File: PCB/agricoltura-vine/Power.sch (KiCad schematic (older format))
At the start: 17 parts, among them T16 1755736, U4 AP63203WU-7, U5 AP63205WU-7

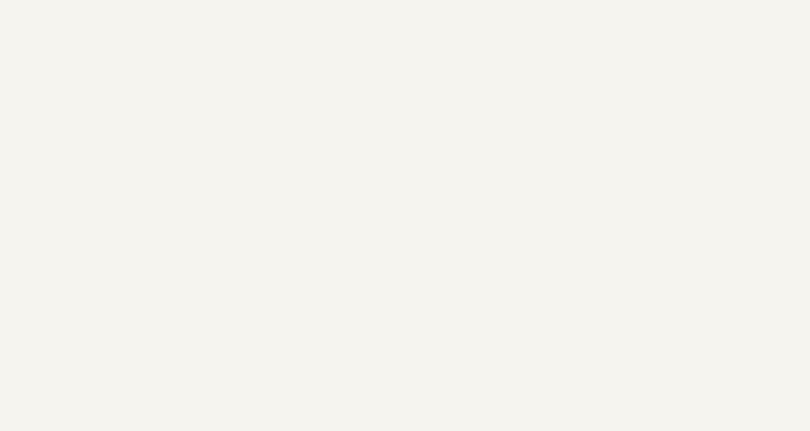
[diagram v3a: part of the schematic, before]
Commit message: Board Size , Connectors and Layout
Changed board size and shape, started layout, swapped connectors over.
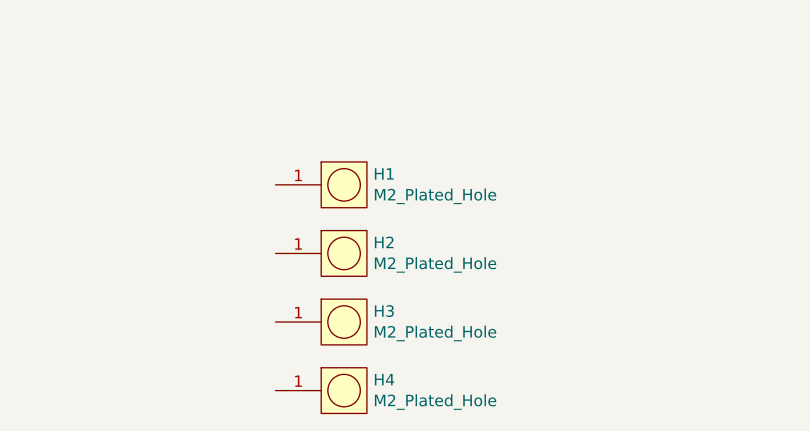
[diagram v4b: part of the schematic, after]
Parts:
- added H1, H2, H3, H4: M2_Plated_Hole, AVR-KiCAD-Lib-Holes_Fasteners:M2_HOLE, symbol AVR-KiCAD-Lib-Holes_Fasteners:M2_Plated_Hole
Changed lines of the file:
@@
 Wire Wire Line
 	4600 3500 4800 3500
+$Comp
+L AVR-KiCAD-Lib-Holes_Fasteners:M2_Plated_Hole H1
+U 1 1 5F227FD5
+P 2750 5600
+F 0 "H1" H 2978 5646 50  0000 L CNN
+F 1 "M2_Plated_Hole" H 2978 5555 50  0000 L CNN
+F 2 "AVR-KiCAD-Lib-Holes_Fasteners:M2_HOLE" H 2750 5600 50  0001 C CNN
+F 3 "" H 2750 5600 50  0001 C CNN
+F 4 "*" H 2850 5850 50  0001 C CNN "Cost QTY: 1"
+F 5 "*" H 2950 5950 50  0001 C CNN "Cost QTY: 1000"
+F 6 "*" H 3050 6050 50  0001 C CNN "Cost QTY: 2500"
+F 7 "*" H 3150 6150 50  0001 C CNN "Cost QTY: 5000"
+F 8 "*" H 3250 6250 50  0001 C CNN "Cost QTY: 10000"
+F 9 "*" H 3350 6350 50  0001 C CNN "MFR"
+F 10 "*" H 3450 6450 50  0001 C CNN "MFR#"
+F 11 "*" H 3550 6550 50  0001 C CNN "Vendor"
+F 12 "*" H 3650 6650 50  0001 C CNN "Vendor #"
+F 13 "*" H 3750 6750 50  0001 C CNN "Designer"
+F 14 "*" H 3850 6850 50  0001 C CNN "Height"
+F 15 "*" H 4950 7950 50  0001 C CNN "Date Created"
+F 16 "*" H 3950 6950 50  0001 C CNN "Date Modified"
+F 17 "*" H 4050 7050 50  0001 C CNN "Lead-Free ?"
+F 18 "*" H 4150 7150 50  0001 C CNN "RoHS Levels"
+F 19 "*" H 4250 7250 50  0001 C CNN "Mounting"
+F 20 "*" H 4350 7350 50  0001 C CNN "Pin Count #"
+F 21 "*" H 4450 7450 50  0001 C CNN "Status"
+F 22 "*" H 4550 7550 50  0001 C CNN "Tolerance"
+F 23 "*" H 4650 7650 50  0001 C CNN "Type"
+F 24 "*" H 4750 7750 50  0001 C CNN "Voltage"
+F 25 "*" H 4850 7900 50  0001 C CNN "Package"
+F 26 "M2 Hole" H 5050 8100 50  0001 C CNN "_Value_"
+F 27 "*" H 5150 8200 50  0001 C CNN "Management_ID"
+F 28 "Plated M2 Screw Hole" H 5150 8200 50  0001 C CNN "Description"
+	1    2750 5600
+	1    0    0    -1
+$EndComp
+$Comp
+L AVR-KiCAD-Lib-Holes_Fasteners:M2_Plated_Hole H2
+U 1 1 5F22DFB9
+P 2750 5900
+F 0 "H2" H 2978 5946 50  0000 L CNN
+F 1 "M2_Plated_Hole" H 2978 5855 50  0000 L CNN
+F 2 "AVR-KiCAD-Lib-Holes_Fasteners:M2_HOLE" H 2750 5900 50  0001 C CNN
+F 3 "" H 2750 5900 50  0001 C CNN
+F 4 "*" H 2850 6150 50  0001 C CNN "Cost QTY: 1"
+F 5 "*" H 2950 6250 50  0001 C CNN "Cost QTY: 1000"
+F 6 "*" H 3050 6350 50  0001 C CNN "Cost QTY: 2500"
+F 7 "*" H 3150 6450 50  0001 C CNN "Cost QTY: 5000"
+F 8 "*" H 3250 6550 50  0001 C CNN "Cost QTY: 10000"
+F 9 "*" H 3350 6650 50  0001 C CNN "MFR"
+F 10 "*" H 3450 6750 50  0001 C CNN "MFR#"
+F 11 "*" H 3550 6850 50  0001 C CNN "Vendor"
+F 12 "*" H 3650 6950 50  0001 C CNN "Vendor #"
+F 13 "*" H 3750 7050 50  0001 C CNN "Designer"
+F 14 "*" H 3850 7150 50  0001 C CNN "Height"
+F 15 "*" H 4950 8250 50  0001 C CNN "Date Created"
+F 16 "*" H 3950 7250 50  0001 C CNN "Date Modified"
+F 17 "*" H 4050 7350 50  0001 C CNN "Lead-Free ?"
+F 18 "*" H 4150 7450 50  0001 C CNN "RoHS Levels"
+F 19 "*" H 4250 7550 50  0001 C CNN "Mounting"
+F 20 "*" H 4350 7650 50  0001 C CNN "Pin Count #"
+F 21 "*" H 4450 7750 50  0001 C CNN "Status"
+F 22 "*" H 4550 7850 50  0001 C CNN "Tolerance"
+F 23 "*" H 4650 7950 50  0001 C CNN "Type"
+F 24 "*" H 4750 8050 50  0001 C CNN "Voltage"
+F 25 "*" H 4850 8200 50  0001 C CNN "Package"
+F 26 "M2 Hole" H 5050 8400 50  0001 C CNN "_Value_"
+F 27 "*" H 5150 8500 50  0001 C CNN "Management_ID"
+F 28 "Plated M2 Screw Hole" H 5150 8500 50  0001 C CNN "Description"
+	1    2750 5900
+	1    0    0    -1
+$EndComp
+$Comp
+L AVR-KiCAD-Lib-Holes_Fasteners:M2_Plated_Hole H3
+U 1 1 5F22E952
+P 2750 6200
+F 0 "H3" H 2978 6246 50  0000 L CNN
+F 1 "M2_Plated_Hole" H 2978 6155 50  0000 L CNN
+F 2 "AVR-KiCAD-Lib-Holes_Fasteners:M2_HOLE" H 2750 6200 50  0001 C CNN
+F 3 "" H 2750 6200 50  0001 C CNN
+F 4 "*" H 2850 6450 50  0001 C CNN "Cost QTY: 1"
+F 5 "*" H 2950 6550 50  0001 C CNN "Cost QTY: 1000"
+F 6 "*" H 3050 6650 50  0001 C CNN "Cost QTY: 2500"
+F 7 "*" H 3150 6750 50  0001 C CNN "Cost QTY: 5000"
+F 8 "*" H 3250 6850 50  0001 C CNN "Cost QTY: 10000"
+F 9 "*" H 3350 6950 50  0001 C CNN "MFR"
+F 10 "*" H 3450 7050 50  0001 C CNN "MFR#"
+F 11 "*" H 3550 7150 50  0001 C CNN "Vendor"
+F 12 "*" H 3650 7250 50  0001 C CNN "Vendor #"
+F 13 "*" H 3750 7350 50  0001 C CNN "Designer"
+F 14 "*" H 3850 7450 50  0001 C CNN "Height"
+F 15 "*" H 4950 8550 50  0001 C CNN "Date Created"
+F 16 "*" H 3950 7550 50  0001 C CNN "Date Modified"
+F 17 "*" H 4050 7650 50  0001 C CNN "Lead-Free ?"
+F 18 "*" H 4150 7750 50  0001 C CNN "RoHS Levels"
+F 19 "*" H 4250 7850 50  0001 C CNN "Mounting"
+F 20 "*" H 4350 7950 50  0001 C CNN "Pin Count #"
+F 21 "*" H 4450 8050 50  0001 C CNN "Status"
+F 22 "*" H 4550 8150 50  0001 C CNN "Tolerance"
+F 23 "*" H 4650 8250 50  0001 C CNN "Type"
+F 24 "*" H 4750 8350 50  0001 C CNN "Voltage"
+F 25 "*" H 4850 8500 50  0001 C CNN "Package"
+F 26 "M2 Hole" H 5050 8700 50  0001 C CNN "_Value_"
+F 27 "*" H 5150 8800 50  0001 C CNN "Management_ID"
+F 28 "Plated M2 Screw Hole" H 5150 8800 50  0001 C CNN "Description"
+	1    2750 6200
+	1    0    0    -1
+$EndComp
+$Comp
+L AVR-KiCAD-Lib-Holes_Fasteners:M2_Plated_Hole H4
+U 1 1 5F22F019
+P 2750 6500
+F 0 "H4" H 2978 6546 50  0000 L CNN
+F 1 "M2_Plated_Hole" H 2978 6455 50  0000 L CNN
+F 2 "AVR-KiCAD-Lib-Holes_Fasteners:M2_HOLE" H 2750 6500 50  0001 C CNN
+F 3 "" H 2750 6500 50  0001 C CNN
+F 4 "*" H 2850 6750 50  0001 C CNN "Cost QTY: 1"
+F 5 "*" H 2950 6850 50  0001 C CNN "Cost QTY: 1000"
+F 6 "*" H 3050 6950 50  0001 C CNN "Cost QTY: 2500"
+F 7 "*" H 3150 7050 50  0001 C CNN "Cost QTY: 5000"
+F 8 "*" H 3250 7150 50  0001 C CNN "Cost QTY: 10000"
+F 9 "*" H 3350 7250 50  0001 C CNN "MFR"
+F 10 "*" H 3450 7350 50  0001 C CNN "MFR#"
+F 11 "*" H 3550 7450 50  0001 C CNN "Vendor"
+F 12 "*" H 3650 7550 50  0001 C CNN "Vendor #"
+F 13 "*" H 3750 7650 50  0001 C CNN "Designer"
+F 14 "*" H 3850 7750 50  0001 C CNN "Height"
+F 15 "*" H 4950 8850 50  0001 C CNN "Date Created"
+F 16 "*" H 3950 7850 50  0001 C CNN "Date Modified"
+F 17 "*" H 4050 7950 50  0001 C CNN "Lead-Free ?"
+F 18 "*" H 4150 8050 50  0001 C CNN "RoHS Levels"
+F 19 "*" H 4250 8150 50  0001 C CNN "Mounting"
+F 20 "*" H 4350 8250 50  0001 C CNN "Pin Count #"
+F 21 "*" H 4450 8350 50  0001 C CNN "Status"
+F 22 "*" H 4550 8450 50  0001 C CNN "Tolerance"
+F 23 "*" H 4650 8550 50  0001 C CNN "Type"
+F 24 "*" H 4750 8650 50  0001 C CNN "Voltage"
+F 25 "*" H 4850 8800 50  0001 C CNN "Package"
+F 26 "M2 Hole" H 5050 9000 50  0001 C CNN "_Value_"
+F 27 "*" H 5150 9100 50  0001 C CNN "Management_ID"
+F 28 "Plated M2 Screw Hole" H 5150 9100 50  0001 C CNN "Description"
+	1    2750 6500
+	1    0    0    -1
+$EndComp
 $EndSCHEMATC

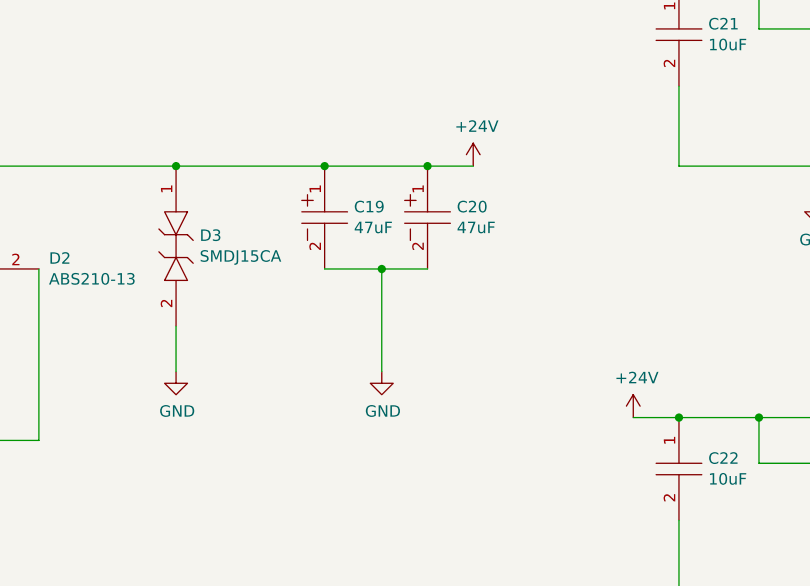
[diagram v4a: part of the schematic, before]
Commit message: Board shape and Rough PLacement
Board shape adjusted to have smaller rounded corners increasing usable space of board shape. Finished rough placement of all the components, no routing yet. Debating connector style and form factor. Right now supports Seeedstudio grove connectors, contemplating Sparkfun Qwiic  and Adafruit Stemma connectors as alternatives or including a variety of all 3.
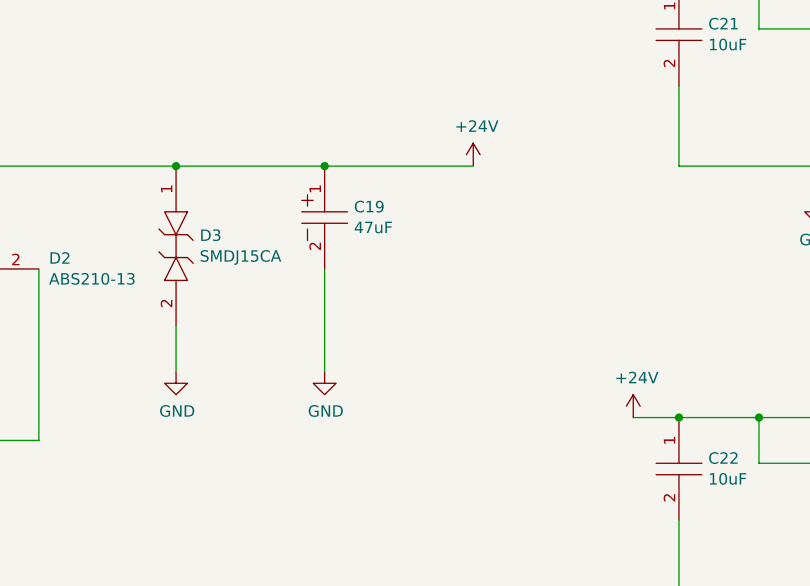
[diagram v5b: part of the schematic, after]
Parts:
- removed C20: UUQ1H470MCL1GS, AVR-KiCAD-Lib-Capacitors:CP_Elec_8x10, symbol AVR-KiCAD-Lib-Capacitors:UUQ1H470MCL1GS
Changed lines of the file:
@@
 $EndComp
 Connection ~ 4350 3050
-Wire Wire Line
-	4350 3050 4800 3050
-$Comp
-L AVR-KiCAD-Lib-Capacitors:UUQ1H470MCL1GS C20
-U 1 1 5EF7802F
-P 4800 3250
-F 0 "C20" V 4779 3378 50  0000 L CNN
-F 1 "UUQ1H470MCL1GS" H 4850 3450 50  0001 C CNN
-F 2 "AVR-KiCAD-Lib-Capacitors:CP_Elec_8x10" H 4600 3250 50  0001 C CNN
-F 3 "https://www.nichicon.co.jp/english/products/pdfs/e-uuq.pdf" H 4700 3350 50  0001 C CNN
-F 4 "1.06000" H 4900 3500 50  0001 C CNN "Cost QTY: 1"
-F 5 "*" H 5000 3600 50  0001 C CNN "Cost QTY: 1000"
-F 6 "*" H 5100 3700 50  0001 C CNN "Cost QTY: 2500"
-F 7 "*" H 5200 3800 50  0001 C CNN "Cost QTY: 5000"
-F 8 "*" H 5300 3900 50  0001 C CNN "Cost QTY: 10000"
-F 9 "Nichicon" H 5400 4000 50  0001 C CNN "MFR"
-F 10 "UUQ1H470MCL1GS" H 5500 4100 50  0001 C CNN "MFR#"
-F 11 "Digikey" H 5600 4200 50  0001 C CNN "Vendor"
-F 12 "493-3212-1-ND" H 5700 4300 50  0001 C CNN "Vendor #"
-F 13 "AVR" H 5800 4400 50  0001 C CNN "Designer"
-F 14 "6.2mm" H 5900 4500 50  0001 C CNN "Height"
-F 15 "12/16/2019" H 7000 5600 50  0001 C CNN "Date Created"
-F 16 "12/16/2019" H 6000 4600 50  0001 C CNN "Date Modified"
-F 17 "Yes" H 6100 4700 50  0001 C CNN "Lead-Free ?"
-F 18 "1" H 6200 4800 50  0001 C CNN "RoHS Levels"
-F 19 "SMT" H 6300 4900 50  0001 C CNN "Mounting"
-F 20 "2" H 6400 5000 50  0001 C CNN "Pin Count #"
-F 21 "Active" H 6500 5100 50  0001 C CNN "Status"
-F 22 "20%" H 6600 5200 50  0001 C CNN "Tolerance"
-F 23 "Alu  Cap Audio" H 6700 5300 50  0001 C CNN "Type"
-F 24 "50V" H 6800 5400 50  0001 C CNN "Voltage"
-F 25 "Radial SMD" H 6900 5550 50  0001 C CNN "Package"
-F 26 "47µF 50V Aluminum Electrolytic Capacitors Radial, Can - SMD 1000 Hrs @ 105°C" H 7300 5950 50  0001 C CNN "Description"
-F 27 "47uF" V 4870 3378 50  0000 L CNN "_Value_"
-F 28 "*" H 7200 5850 50  0001 C CNN "Management_ID"
-	1    4800 3250
-	0    1    1    0
-$EndComp
-Connection ~ 4800 3050
-Wire Wire Line
-	4800 3050 5000 3050
 $Comp
 L power:GND #PWR030
 U 1 1 5EF78FAF
-P 4600 3950
-F 0 "#PWR030" H 4600 3700 50  0001 C CNN
-F 1 "GND" H 4605 3777 50  0000 C CNN
-F 2 "" H 4600 3950 50  0001 C CNN
-F 3 "" H 4600 3950 50  0001 C CNN
-	1    4600 3950
+P 4350 3950
+F 0 "#PWR030" H 4350 3700 50  0001 C CNN
+F 1 "GND" H 4355 3777 50  0000 C CNN
+F 2 "" H 4350 3950 50  0001 C CNN
+F 3 "" H 4350 3950 50  0001 C CNN
+	1    4350 3950
 	1    0    0    -1
 $EndComp
 Wire Wire Line
-	4350 3500 4600 3500
-Wire Wire Line
-	4600 3950 4600 3500
-Connection ~ 4600 3500
-Wire Wire Line
-	4600 3500 4800 3500
+	4350 3950 4350 3500
 $Comp
 L AVR-KiCAD-Lib-Holes_Fasteners:M2_Plated_Hole H1
@@
 	1    0    0    -1
 $EndComp
+Wire Wire Line
+	4350 3050 5000 3050
 $EndSCHEMATC

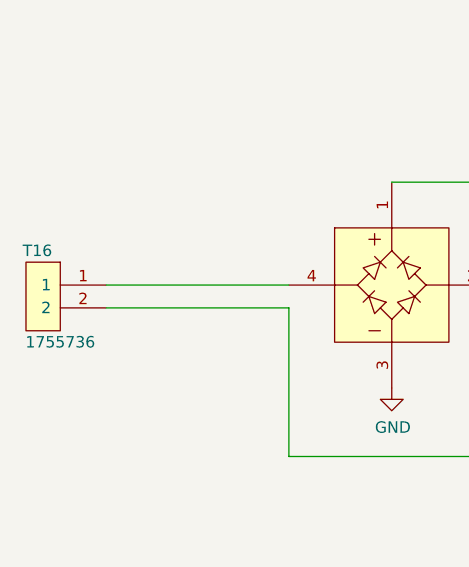
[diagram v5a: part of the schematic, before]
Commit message: Route Started Connectors Changed
Changed to QWIIC style connectors and adjusted pinning of RJ45s, but switching to screw terminal header in next commit. THis is a backup
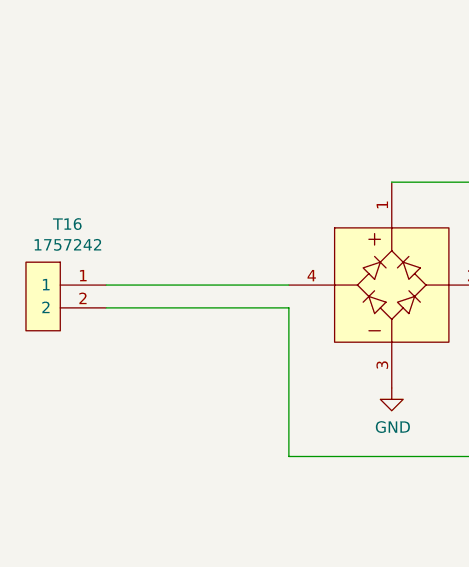
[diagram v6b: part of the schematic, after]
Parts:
- removed T16: 1755736, growbox-KiCAD-Connectors:PhoenixContact_MSTBVA-G_02x5.08mm_Vertical, symbol AVR-KiCAD-Lib-Connectors:1755736
- added T16: 1757242, AVR-KiCAD-Lib-Connectors:PhoenixContact_MSTBA-G_02x5.08mm_Angled, symbol AVR-KiCAD-Lib-Connectors:1757242
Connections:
- net at D2.4: now also T16.1
- net at D2.2: now also T16.2
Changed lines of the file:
@@
 $EndDescr
-$Comp
-L AVR-KiCAD-Lib-Connectors:1755736 T16
-U 1 1 5EEBB45B
-P 1200 3300
-F 0 "T16" H 1300 3250 50  0000 C CNN
-F 1 "1755736" H 1200 2850 50  0000 C CNN
-F 2 "growbox-KiCAD-Connectors:PhoenixContact_MSTBVA-G_02x5.08mm_Vertical" H 1000 3300 50  0001 C CNN
-F 3 "https://media.digikey.com/pdf/Data%20Sheets/Phoenix%20Contact%20PDFs/1755794.pdf" H 1100 3400 50  0001 C CNN
-F 4 "0.64000" H 1300 3550 50  0001 C CNN "Cost QTY: 1"
-F 5 "0.45518" H 1400 3650 50  0001 C CNN "Cost QTY: 1000"
-F 6 "0.43375" H 1500 3750 50  0001 C CNN "Cost QTY: 2500"
-F 7 "0.40698" H 1600 3850 50  0001 C CNN "Cost QTY: 5000"
-F 8 "*" H 1700 3950 50  0001 C CNN "Cost QTY: 10000"
-F 9 "Phoenix Contact" H 1800 4050 50  0001 C CNN "MFR"
-F 10 "1755736" H 1900 4150 50  0001 C CNN "MFR#"
-F 11 "Digikey" H 2000 4250 50  0001 C CNN "Vendor"
-F 12 "277-1150-ND" H 2100 4350 50  0001 C CNN "Vendor #"
-F 13 "AVR" H 2200 4450 50  0001 C CNN "Designer"
-F 14 "12mm" H 2300 4550 50  0001 C CNN "Height"
-F 15 "3/11/2020" H 3400 5650 50  0001 C CNN "Date Created"
-F 16 "3/11/2020" H 2400 4650 50  0001 C CNN "Date Modified"
-F 17 "Yes" H 2500 4750 50  0001 C CNN "Lead-Free ?"
-F 18 "1" H 2600 4850 50  0001 C CNN "RoHS Levels"
-F 19 "ThroughHole" H 2700 4950 50  0001 C CNN "Mounting"
-F 20 "2" H 2800 5050 50  0001 C CNN "Pin Count #"
-F 21 "Active" H 2900 5150 50  0001 C CNN "Status"
-F 22 "*" H 3000 5250 50  0001 C CNN "Tolerance"
-F 23 "Connector, Terminal Block " H 3100 5350 50  0001 C CNN "Type"
-F 24 "300V" H 3200 5450 50  0001 C CNN "Voltage"
-F 25 "*" H 3300 5600 50  0001 C CNN "Package"
-F 26 "2 Position Terminal Block Header, Male Pins, Shrouded (4 Side) 0.200\" (5.08mm) Vertical  Through Hole" H 3700 6000 50  0001 C CNN "Description"
-F 27 "1755736" H 3500 5800 50  0001 C CNN "_Value_"
-F 28 "*" H 3600 5900 50  0001 C CNN "Management_ID"
-	1    1200 3300
-	-1   0    0    -1
-$EndComp
 $Comp
 L AVR-KiCAD-Lib-Diodes:ABS210-13 D2
@@
 Wire Wire Line
 	4350 3050 5000 3050
+$Comp
+L AVR-KiCAD-Lib-Connectors:1757242 T16
+U 1 1 5EF359F8
+P 1200 3300
+F 0 "T16" H 1167 3365 50  0000 C CNN
+F 1 "1757242" H 1167 3274 50  0000 C CNN
+F 2 "AVR-KiCAD-Lib-Connectors:PhoenixContact_MSTBA-G_02x5.08mm_Angled" H 1000 3300 50  0001 C CNN
+F 3 "https://media.digikey.com/pdf/Data%20Sheets/Phoenix%20Contact%20PDFs/1757242.pdf" H 1100 3400 50  0001 C CNN
+F 4 "0.64000" H 1300 3550 50  0001 C CNN "Cost QTY: 1"
+F 5 "0.45518" H 1400 3650 50  0001 C CNN "Cost QTY: 1000"
+F 6 "0.43375" H 1500 3750 50  0001 C CNN "Cost QTY: 2500"
+F 7 "0.40698" H 1600 3850 50  0001 C CNN "Cost QTY: 5000"
+F 8 "*" H 1700 3950 50  0001 C CNN "Cost QTY: 10000"
+F 9 "Phoenix Contact" H 1800 4050 50  0001 C CNN "MFR"
+F 10 "1757242" H 1900 4150 50  0001 C CNN "MFR#"
+F 11 "Digikey" H 2000 4250 50  0001 C CNN "Vendor"
+F 12 "277-1106-ND" H 2100 4350 50  0001 C CNN "Vendor #"
+F 13 "AVR" H 2200 4450 50  0001 C CNN "Designer"
+F 14 "12mm" H 2300 4550 50  0001 C CNN "Height"
+F 15 "6/20/2020" H 3400 5650 50  0001 C CNN "Date Created"
+F 16 "6/20/2020" H 2400 4650 50  0001 C CNN "Date Modified"
+F 17 "Yes" H 2500 4750 50  0001 C CNN "Lead-Free ?"
+F 18 "1" H 2600 4850 50  0001 C CNN "RoHS Levels"
+F 19 "ThroughHole" H 2700 4950 50  0001 C CNN "Mounting"
+F 20 "2" H 2800 5050 50  0001 C CNN "Pin Count #"
+F 21 "Active" H 2900 5150 50  0001 C CNN "Status"
+F 22 "*" H 3000 5250 50  0001 C CNN "Tolerance"
+F 23 "Connector" H 3100 5350 50  0001 C CNN "Type"
+F 24 "300V" H 3200 5450 50  0001 C CNN "Voltage"
+F 25 "*" H 3300 5600 50  0001 C CNN "Package"
+F 26 "2 Position Terminal Block Header, Male Pins, Shrouded (4 Side) 0.200\" (5.08mm) 90°, Right Angle  Through Hole" H 3700 6000 50  0001 C CNN "Description"
+F 27 "1757242" H 3500 5800 50  0001 C CNN "_Value_"
+F 28 "*" H 3600 5900 50  0001 C CNN "Management_ID"
+	1    1200 3300
+	-1   0    0    -1
+$EndComp
 $EndSCHEMATC
